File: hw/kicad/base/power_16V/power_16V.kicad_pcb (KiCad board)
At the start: 2 copper layers, 45 x 45 mm, 38 parts, among them J1 USB_B_Micro, J3 TOP, J4 BUTTOM, U1 LM2596S-5, U2 LM1117MP-3.3, U3 CP2104, U4 ACS712xLCTR-05B

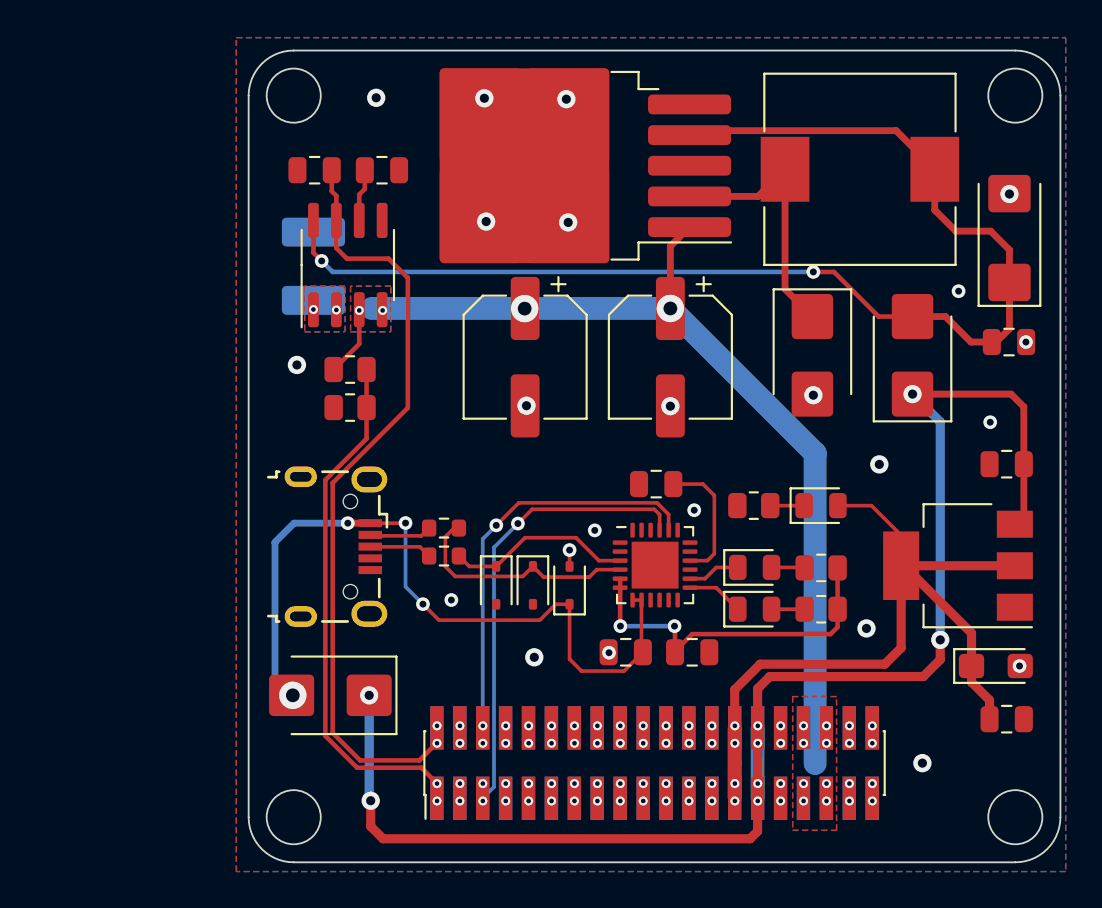
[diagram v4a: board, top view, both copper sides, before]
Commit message: 更新power16v一些错误
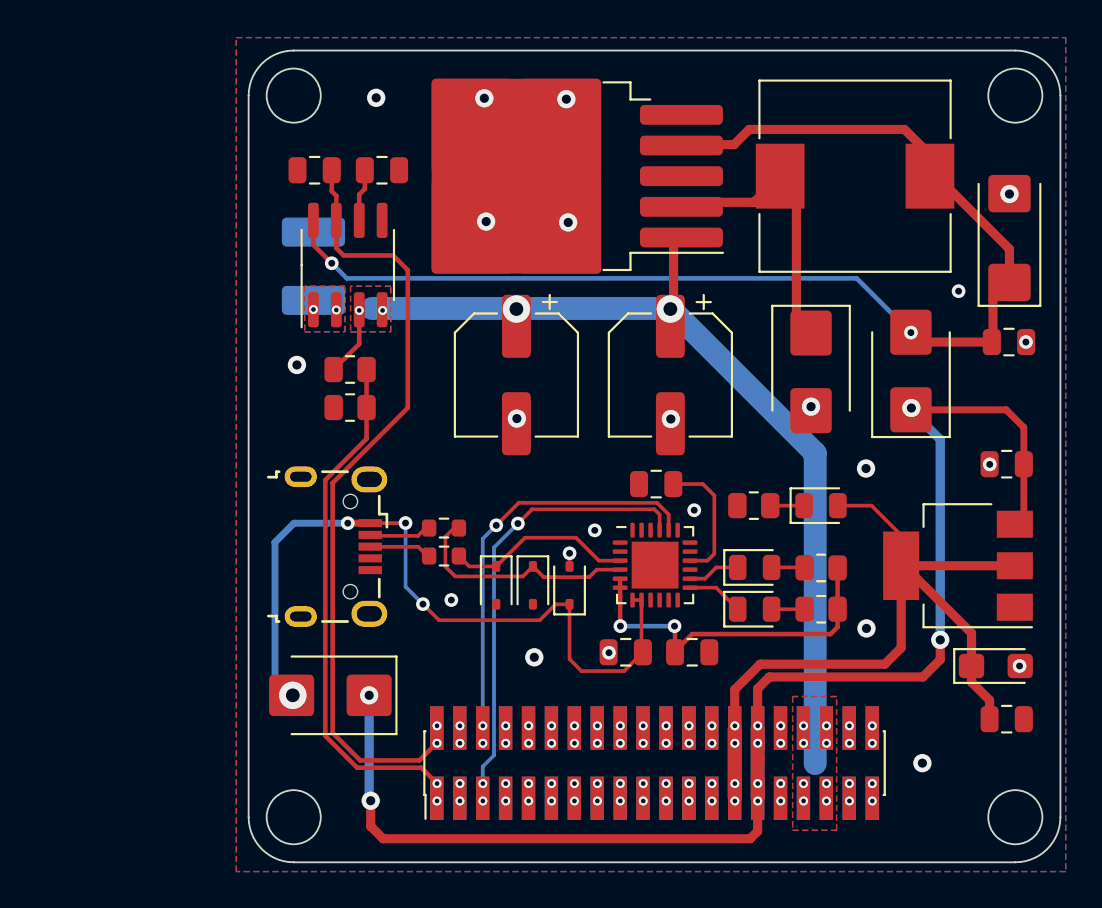
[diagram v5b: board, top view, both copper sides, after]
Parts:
- moved C10 1.10 mm to (65.6, 50.7)
- moved C1 0.99 mm to (74.1, 50.7)
- moved D3 0.92 mm to (81.9, 50.5)
- moved D6 0.87 mm to (87.4, 50.5)
- moved U1 0.73 mm to (67.1, 39.7)
- moved L1 0.47 mm to (84.3, 39.7)
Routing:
- net +5V: track 82.5 -> 80.7 mm
- net Net-(D3-K): track 14.7 -> 15.6 mm
- net +BATT: track 54.2 -> 53.4 mm

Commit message: 更新USB micro 为优信的封装
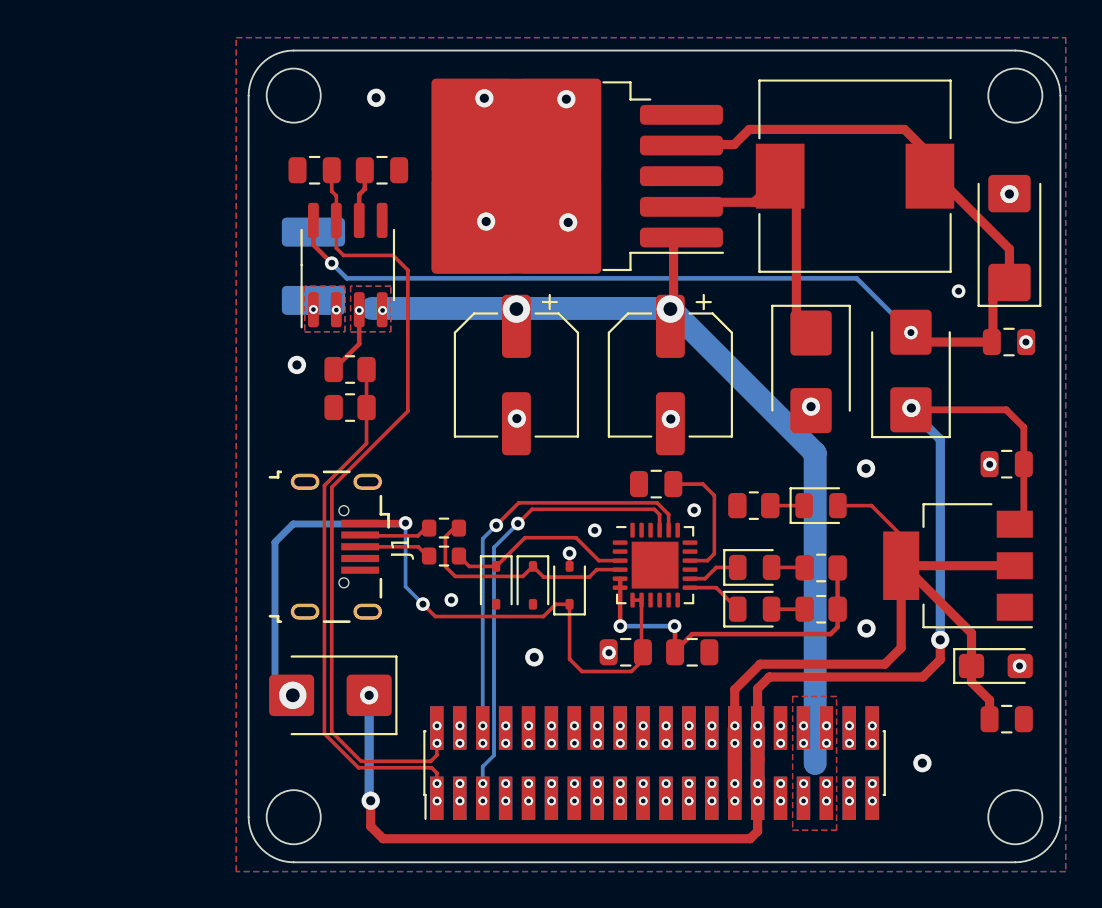
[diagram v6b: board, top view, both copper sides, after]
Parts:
- J1: footprint Connector_USB:USB_Micro-B_Wuerth_629105150521 -> USB_Micro-B_YouCee:USB_Micro-B_YouCee
- R3: value 10k -> 1k
- R4, R5: value 100 -> 1k
- moved J1 0.09 mm to (55.7, 60.2)
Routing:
- net Net-(D1-A): track 41.6 -> 44.2 mm, vias 4 -> 3
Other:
- board text added: "Pindar v1.2 (Base) power16v v1.3"
- board text removed: "Pindar v1.2 (Base) power16v v1.2"
